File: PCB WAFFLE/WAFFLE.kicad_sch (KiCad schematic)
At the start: 24 parts, among them IC1 STM32L412KBT6, J2 FTSH-107-01-L-DV, J7 Conn_01x03_Male

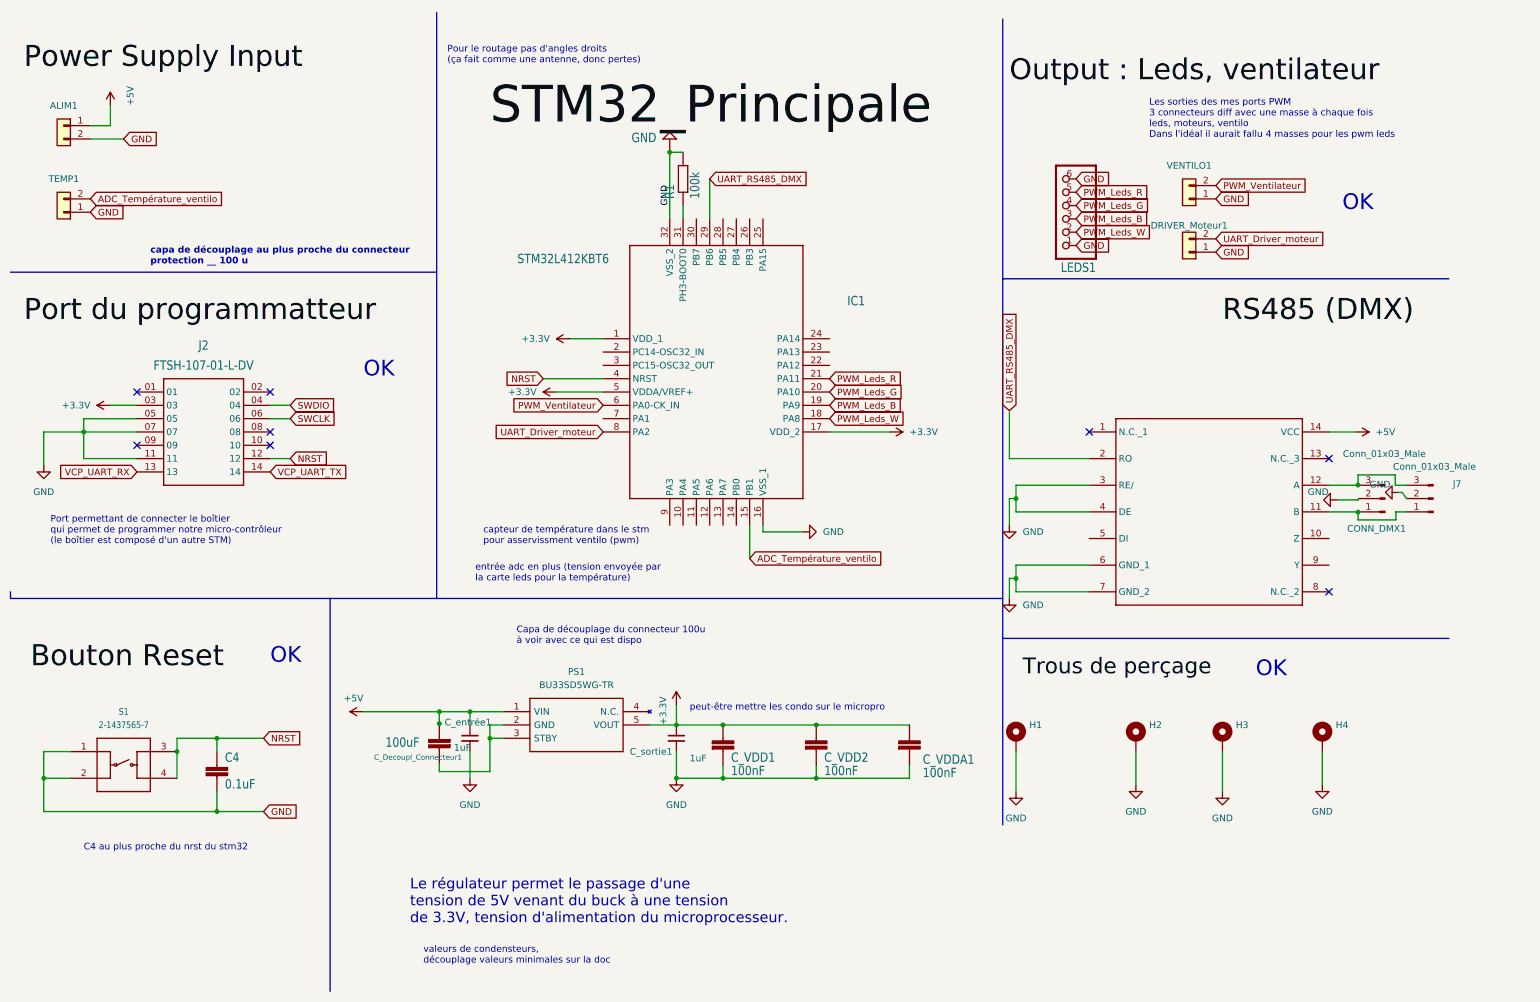
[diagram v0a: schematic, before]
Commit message: Add files via upload
Version du 28/02 du pcb de contrôle (ajout d'un système de driver pour le ventilo)
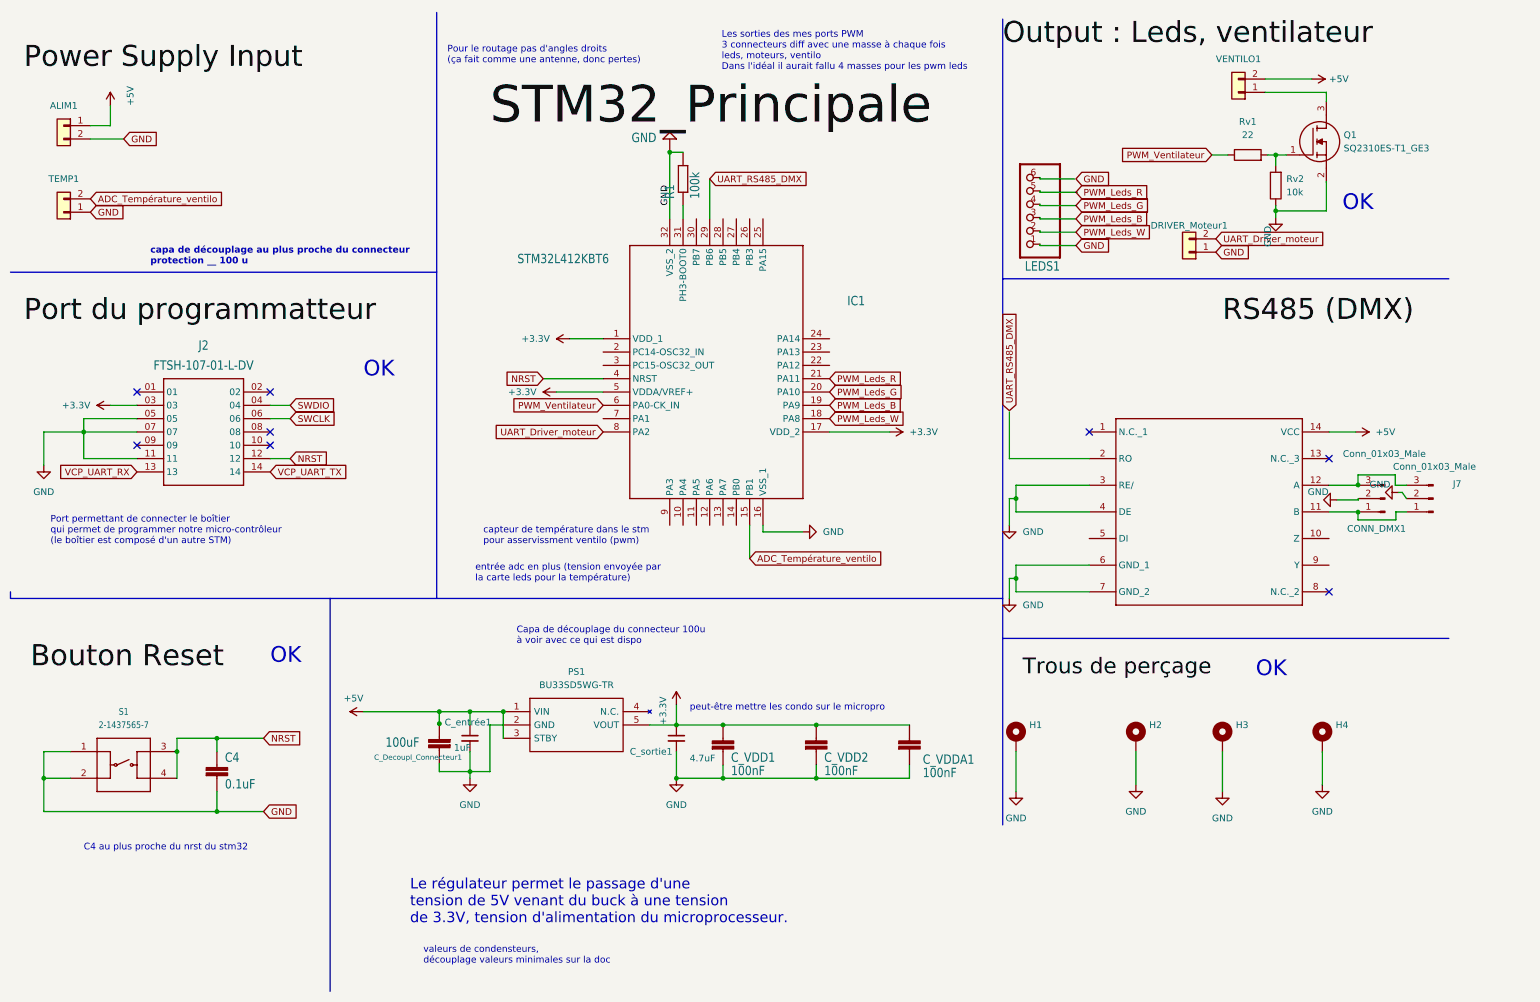
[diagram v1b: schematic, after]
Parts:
- added Q1: SQ2310ES-T1_GE3, SOT95P237X112-3N, symbol ProjetENSEA:SQ2310ES-T1_GE3
- added Rv1: 22, stm32l021:R0603, symbol Device:R
- added Rv2: 10k, stm32l021:R0603, symbol Device:R
- C_sortie1: value 1uF -> 4.7uF
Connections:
- net +5V: now also PS1.3 (STBY), VENTILO1.2 (Pin_2)
- net GND: now also C_Decoupl_Connecteur1.1, PS1.2 (GND), Q1.2, Rv2.1; no longer LEDS1.6, VENTILO1.1 (Pin_1)
- net PWM_Ventilateur: now also Rv1.1; no longer VENTILO1.2 (Pin_2)
- new net: Q1.1, Rv1.2, Rv2.2
- new net: Q1.3, VENTILO1.1 (Pin_1)
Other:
- moved on the sheet: LEDS1, VENTILO1

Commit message: Add files via upload
Après remarques du professeur : Erreurs de routage (CRC) corrigées, changement de l'empreinte du connecteur LED par un jst (et correction des empreintes connecteurs DMX), connexion de l'uart pour la sonde (oubli).
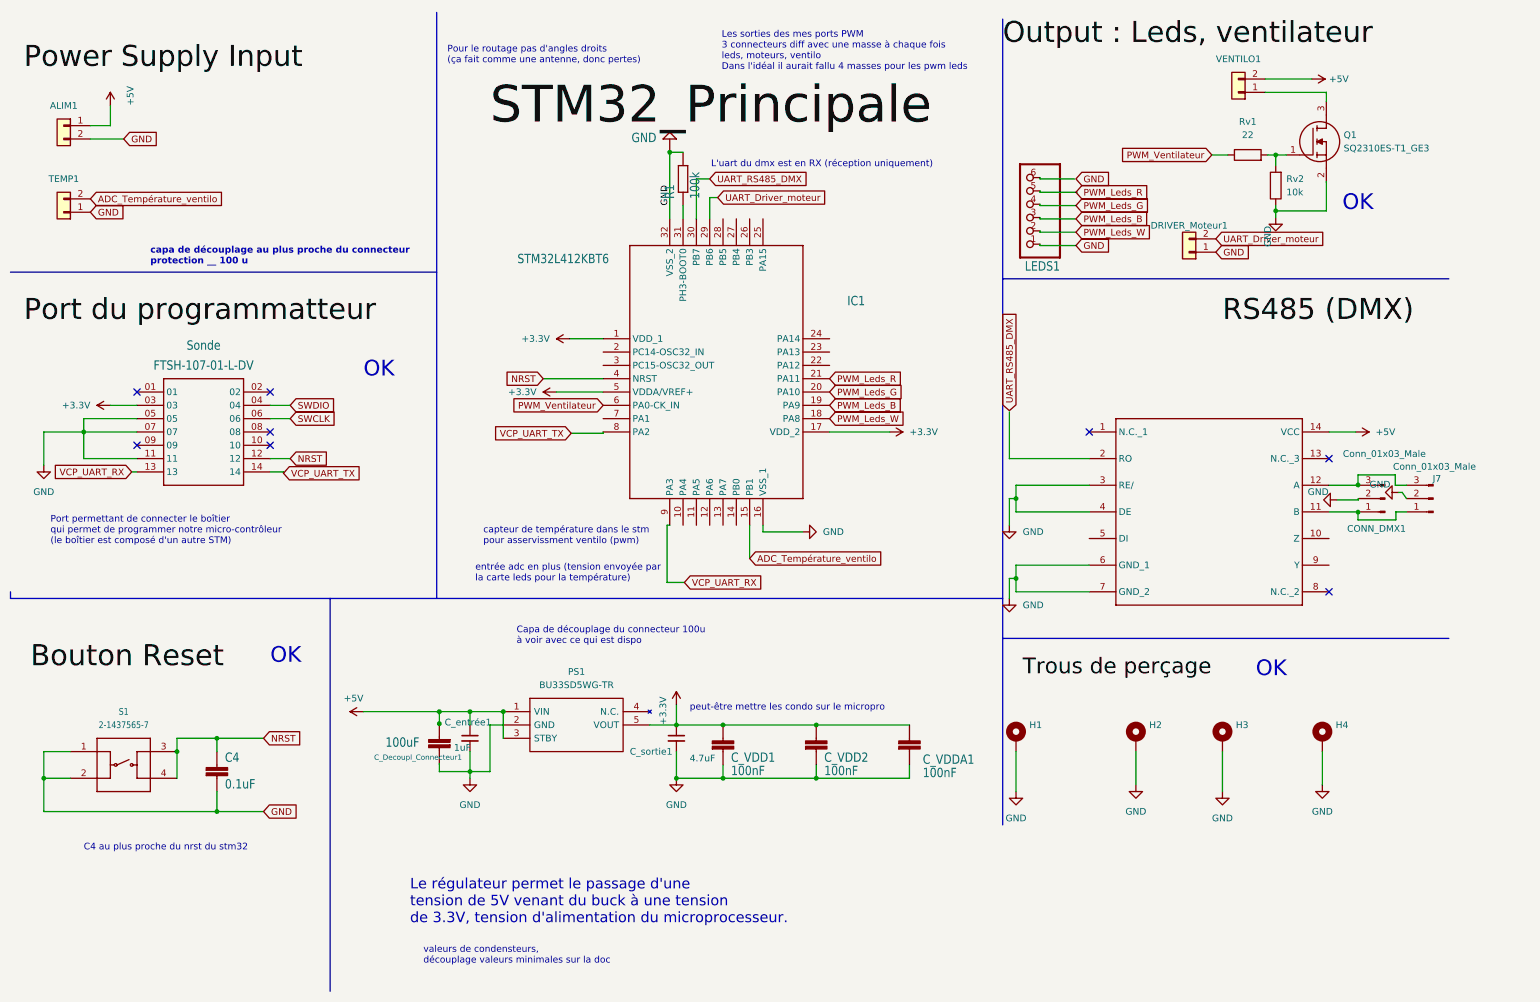
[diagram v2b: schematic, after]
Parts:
- CONN_DMX1, J7: footprint Connector_JST:JST_XH_B3B-XH-AM_1x03_P2.50mm_Vertical -> Connector_JST:JST_XH_B3B-XH-A_1x03_P2.50mm_Vertical
- LEDS1: footprint stm32l021:1X06 -> Connector_JST:JST_XH_B6B-XH-A_1x06_P2.50mm_Vertical
- renumbered J2 to Sonde
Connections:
- net UART_Driver_moteur: now also IC1.29 (PB6); no longer IC1.8 (PA2)
- net UART_RS485_DMX: now also IC1.30 (PB7); no longer IC1.29 (PB6)
- net VCP_UART_RX: now also IC1.9 (PA3)
- net VCP_UART_TX: now also IC1.8 (PA2)
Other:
- note added: "L'uart du dmx est en RX (réception uniquement)"
